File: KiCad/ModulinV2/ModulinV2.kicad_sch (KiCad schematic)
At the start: 0 parts

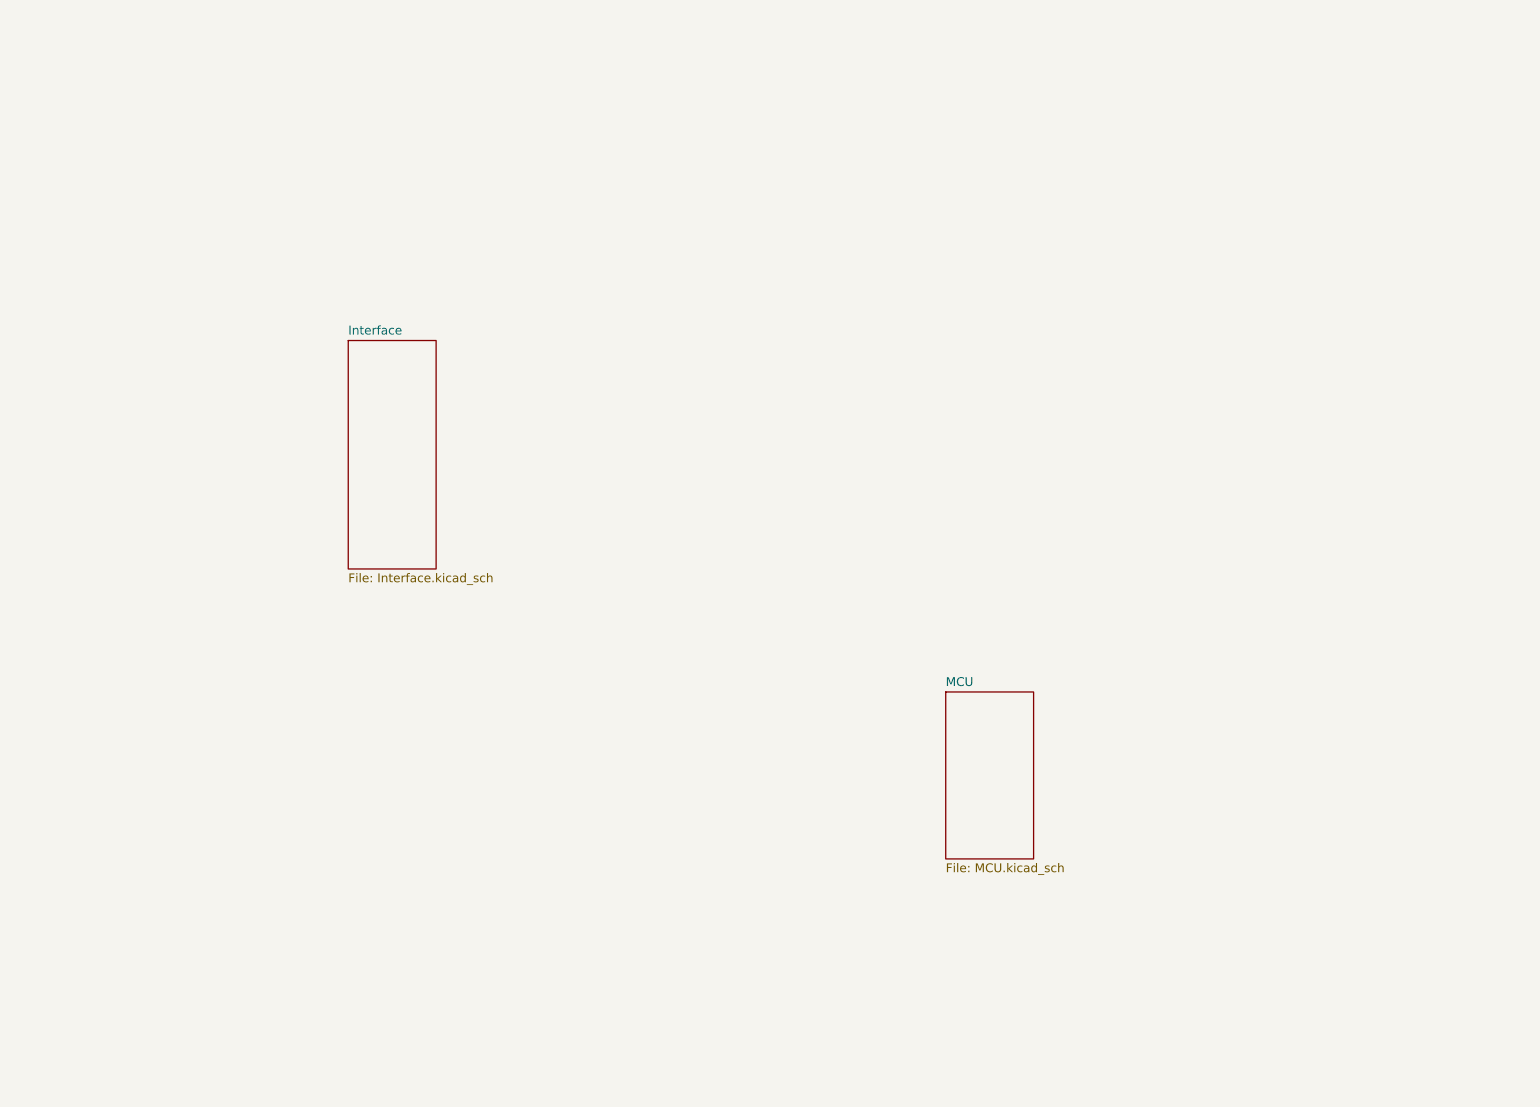
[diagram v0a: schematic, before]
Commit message: Added initial schematic and components for interface
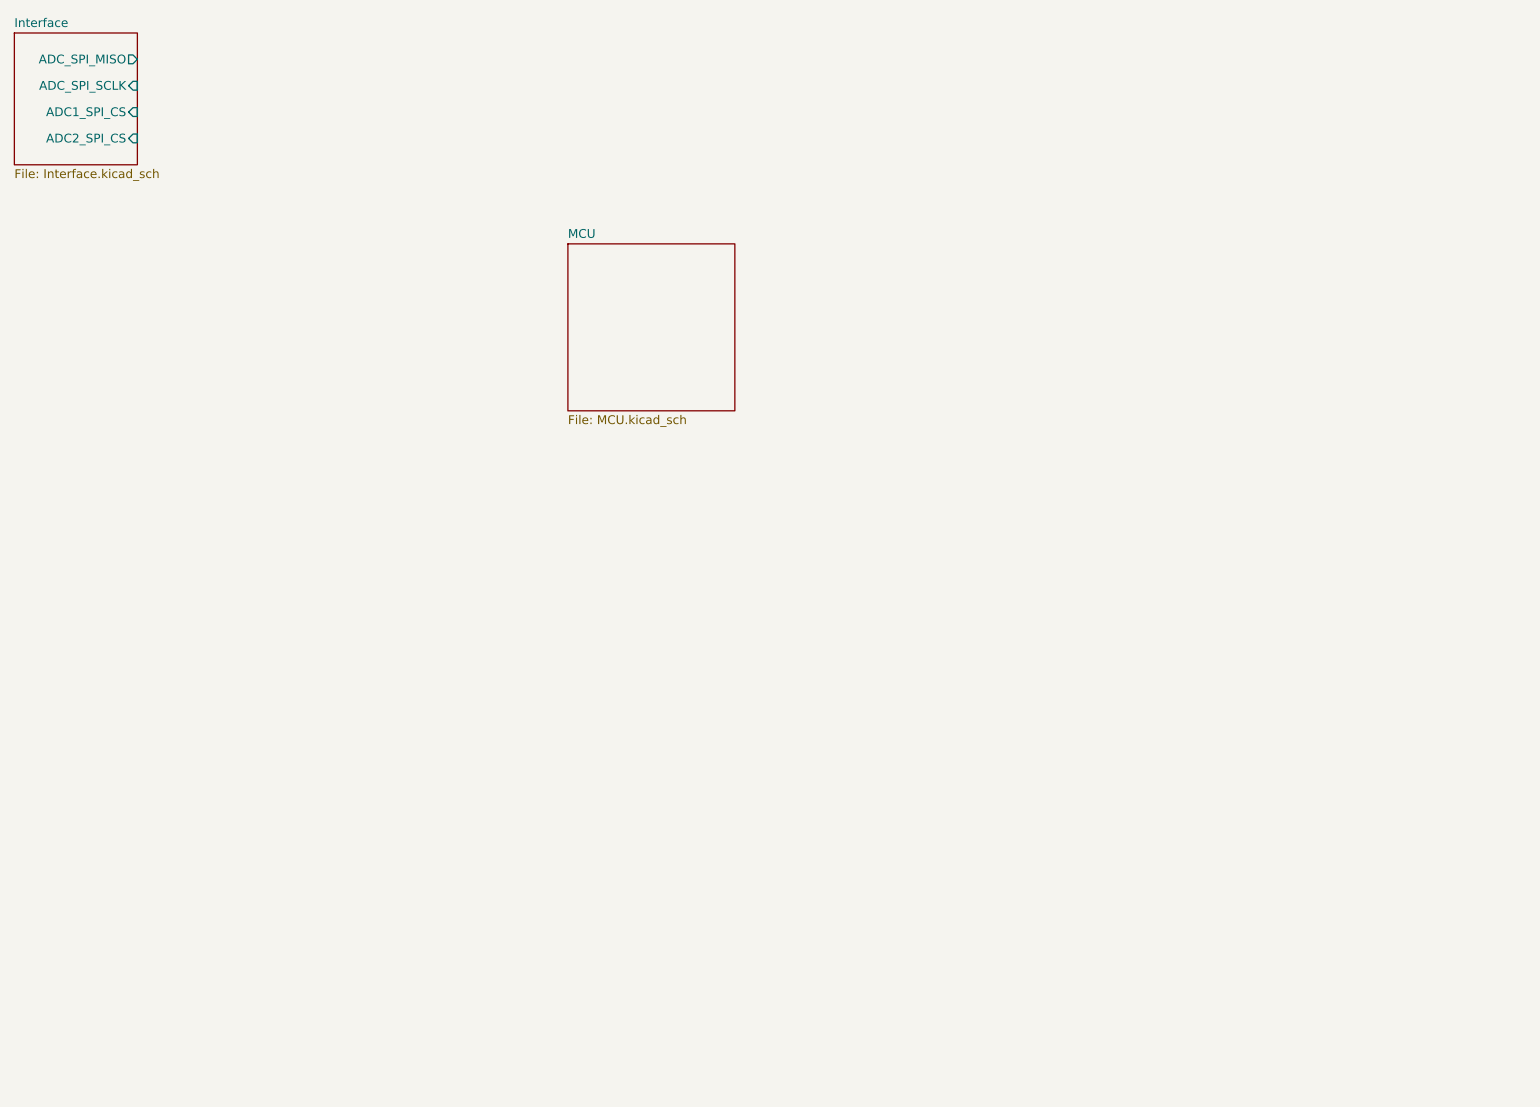
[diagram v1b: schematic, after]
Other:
- sheet Interface ports: added ADC1_SPI_CS, ADC2_SPI_CS, ADC_SPI_MISO, ADC_SPI_SCLK; removed none
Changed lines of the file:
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@@
 	)
 	(sheet
-		(at 69.85 72.39)
-		(size 12.7 33.02)
+		(at 21.59 27.94)
+		(size 17.78 19.05)
 		(exclude_from_sim no)
 		(in_bom yes)
@@
 		)
 		(property "Sheetname" "Interface"
-			(at 69.85 71.6784 0)
+			(at 21.59 27.2284 0)
 			(effects
 				(font
@@
 		)
 		(property "Sheetfile" "Interface.kicad_sch"
-			(at 69.85 105.9946 0)
+			(at 21.59 47.5746 0)
 			(effects
 				(font
@@
 				)
 				(justify left top)
+			)
+		)
+		(pin "ADC1_SPI_CS" input
+			(at 39.37 39.37 0)
+			(effects
+				(font
+					(size 1.27 1.27)
+				)
+				(justify right)
+			)
+		)
+		(pin "ADC_SPI_SCLK" input
+			(at 39.37 35.56 0)
+			(effects
+				(font
+					(size 1.27 1.27)
+				)
+				(justify right)
+			)
+		)
+		(pin "ADC_SPI_MISO" output
+			(at 39.37 31.75 0)
+			(effects
+				(font
+					(size 1.27 1.27)
+				)
+				(justify right)
+			)
+		)
+		(pin "ADC2_SPI_CS" input
+			(at 39.37 43.18 0)
+			(effects
+				(font
+					(size 1.27 1.27)
+				)
+				(justify right)
 			)
 		)
@@
 	)
 	(sheet
-		(at 156.21 123.19)
-		(size 12.7 24.13)
+		(at 101.6 58.42)
+		(size 24.13 24.13)
 		(exclude_from_sim no)
 		(in_bom yes)
@@
 		)
 		(property "Sheetname" "MCU"
-			(at 156.21 122.4784 0)
+			(at 101.6 57.7084 0)
 			(show_name yes)
 			(effects
@@
 		)
 		(property "Sheetfile" "MCU.kicad_sch"
-			(at 156.21 147.9046 0)
+			(at 101.6 83.1346 0)
 			(effects
 				(font

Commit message: Semi-finished interface schematic
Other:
- sheet Interface ports: added DAC1_SPI_CS, DAC1_SPI_MOSI, DAC2_SPI_CS, DAC_SPI_CLK, INTERFACE_PITCH_CV1, INTERFACE_PITCH_CV2, NOTE_TRIG1, NOTE_TRIG2, PRESSURE_CV1, PRESSURE_CV2; removed none
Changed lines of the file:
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@@
 	)
 	(sheet
-		(at 21.59 27.94)
-		(size 17.78 19.05)
+		(at 21.59 29.21)
+		(size 43.18 38.1)
 		(exclude_from_sim no)
 		(in_bom yes)
@@
 		)
 		(property "Sheetname" "Interface"
-			(at 21.59 27.2284 0)
+			(at 21.59 28.4984 0)
 			(effects
 				(font
@@
 		)
 		(property "Sheetfile" "Interface.kicad_sch"
-			(at 21.59 47.5746 0)
+			(at 21.59 67.8946 0)
 			(effects
 				(font
@@
 		)
 		(pin "ADC1_SPI_CS" input
-			(at 39.37 39.37 0)
+			(at 64.77 39.37 0)
 			(effects
 				(font
@@
 		)
 		(pin "ADC_SPI_SCLK" input
-			(at 39.37 35.56 0)
+			(at 64.77 35.56 0)
 			(effects
 				(font
@@
 		)
 		(pin "ADC_SPI_MISO" output
-			(at 39.37 31.75 0)
+			(at 64.77 31.75 0)
 			(effects
 				(font
@@
 		)
 		(pin "ADC2_SPI_CS" input
-			(at 39.37 43.18 0)
+			(at 64.77 43.18 0)
 			(effects
 				(font
@@
 				)
 				(justify right)
+			)
+		)
+		(pin "PRESSURE_CV1" output
+			(at 64.77 50.8 0)
+			(effects
+				(font
+					(size 1.27 1.27)
+				)
+				(justify right)
+			)
+		)
+		(pin "DAC1_SPI_MOSI" input
+			(at 21.59 31.75 180)
+			(effects
+				(font
+					(size 1.27 1.27)
+				)
+				(justify left)
+			)
+		)
+		(pin "INTERFACE_PITCH_CV2" output
+			(at 21.59 54.61 180)
+			(effects
+				(font
+					(size 1.27 1.27)
+				)
+				(justify left)
+			)
+		)
+		(pin "PRESSURE_CV2" output
+			(at 64.77 54.61 0)
+			(effects
+				(font
+					(size 1.27 1.27)
+				)
+				(justify right)
+			)
+		)
+		(pin "DAC1_SPI_CS" input
+			(at 21.59 39.37 180)
+			(effects
+				(font
+					(size 1.27 1.27)
+				)
+				(justify left)
+			)
+		)
+		(pin "NOTE_TRIG2" output
+			(at 64.77 64.77 0)
+			(effects
+				(font
+					(size 1.27 1.27)
+				)
+				(justify right)
+			)
+		)
+		(pin "DAC2_SPI_CS" input
+			(at 21.59 43.18 180)
+			(effects
+				(font
+					(size 1.27 1.27)
+				)
+				(justify left)
+			)
+		)
+		(pin "NOTE_TRIG1" output
+			(at 64.77 60.96 0)
+			(effects
+				(font
+					(size 1.27 1.27)
+				)
+				(justify right)
+			)
+		)
+		(pin "DAC_SPI_CLK" input
+			(at 21.59 35.56 180)
+			(effects
+				(font
+					(size 1.27 1.27)
+				)
+				(justify left)
+			)
+		)
+		(pin "INTERFACE_PITCH_CV1" output
+			(at 21.59 50.8 180)
+			(effects
+				(font
+					(size 1.27 1.27)
+				)
+				(justify left)
 			)
 		)
@@
 	)
 	(sheet
-		(at 101.6 58.42)
+		(at 102.87 36.83)
 		(size 24.13 24.13)
 		(exclude_from_sim no)
@@
 		)
 		(property "Sheetname" "MCU"
-			(at 101.6 57.7084 0)
+			(at 102.87 36.1184 0)
 			(show_name yes)
 			(effects
@@
 		)
 		(property "Sheetfile" "MCU.kicad_sch"
-			(at 101.6 83.1346 0)
+			(at 102.87 61.5446 0)
 			(effects
 				(font

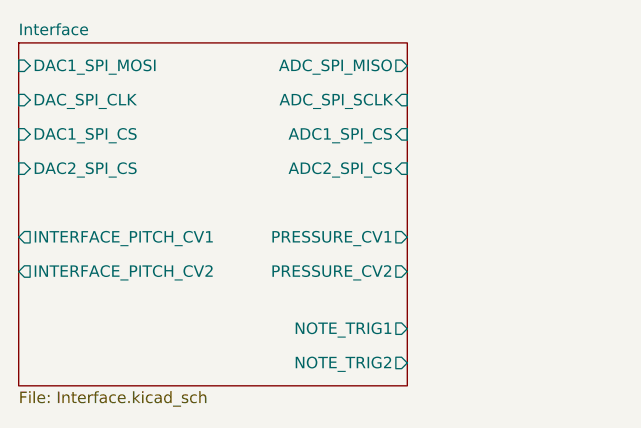
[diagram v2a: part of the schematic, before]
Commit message: Added CubeIDE folder and mapped out initial SPI pins
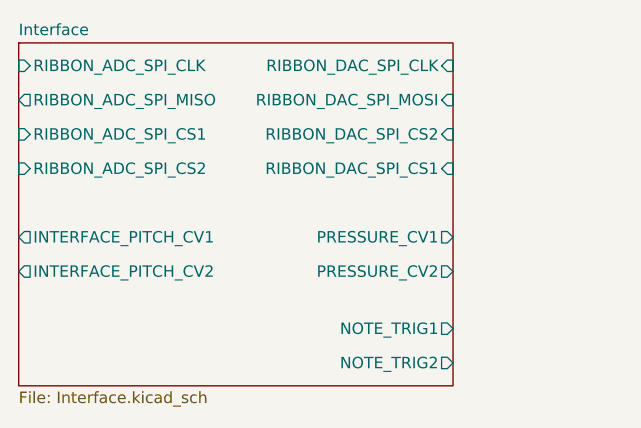
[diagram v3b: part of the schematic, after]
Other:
- sheet Interface ports: added RIBBON_ADC_SPI_CLK, RIBBON_ADC_SPI_CS1, RIBBON_ADC_SPI_CS2, RIBBON_ADC_SPI_MISO, RIBBON_DAC_SPI_CLK, RIBBON_DAC_SPI_CS1, RIBBON_DAC_SPI_CS2, RIBBON_DAC_SPI_MOSI; removed ADC1_SPI_CS, ADC2_SPI_CS, ADC_SPI_MISO, ADC_SPI_SCLK, DAC1_SPI_CS, DAC1_SPI_MOSI, DAC2_SPI_CS, DAC_SPI_CLK
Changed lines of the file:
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@@
 	(sheet
 		(at 21.59 29.21)
-		(size 43.18 38.1)
+		(size 48.26 38.1)
 		(exclude_from_sim no)
 		(in_bom yes)
@@
 			)
 		)
-		(pin "ADC1_SPI_CS" input
-			(at 64.77 39.37 0)
+		(pin "PRESSURE_CV1" output
+			(at 69.85 50.8 0)
 			(effects
 				(font
@@
 				)
 				(justify right)
-			)
-		)
-		(pin "ADC_SPI_SCLK" input
-			(at 64.77 35.56 0)
-			(effects
-				(font
-					(size 1.27 1.27)
-				)
-				(justify right)
-			)
-		)
-		(pin "ADC_SPI_MISO" output
-			(at 64.77 31.75 0)
-			(effects
-				(font
-					(size 1.27 1.27)
-				)
-				(justify right)
-			)
-		)
-		(pin "ADC2_SPI_CS" input
-			(at 64.77 43.18 0)
-			(effects
-				(font
-					(size 1.27 1.27)
-				)
-				(justify right)
-			)
-		)
-		(pin "PRESSURE_CV1" output
-			(at 64.77 50.8 0)
-			(effects
-				(font
-					(size 1.27 1.27)
-				)
-				(justify right)
-			)
-		)
-		(pin "DAC1_SPI_MOSI" input
-			(at 21.59 31.75 180)
-			(effects
-				(font
-					(size 1.27 1.27)
-				)
-				(justify left)
 			)
 		)
@@
 		)
 		(pin "PRESSURE_CV2" output
-			(at 64.77 54.61 0)
+			(at 69.85 54.61 0)
 			(effects
 				(font
@@
 			)
 		)
-		(pin "DAC1_SPI_CS" input
+		(pin "NOTE_TRIG2" output
+			(at 69.85 64.77 0)
+			(effects
+				(font
+					(size 1.27 1.27)
+				)
+				(justify right)
+			)
+		)
+		(pin "NOTE_TRIG1" output
+			(at 69.85 60.96 0)
+			(effects
+				(font
+					(size 1.27 1.27)
+				)
+				(justify right)
+			)
+		)
+		(pin "INTERFACE_PITCH_CV1" output
+			(at 21.59 50.8 180)
+			(effects
+				(font
+					(size 1.27 1.27)
+				)
+				(justify left)
+			)
+		)
+		(pin "RIBBON_ADC_SPI_CLK" input
+			(at 21.59 31.75 180)
+			(effects
+				(font
+					(size 1.27 1.27)
+				)
+				(justify left)
+			)
+		)
+		(pin "RIBBON_DAC_SPI_CLK" input
+			(at 69.85 31.75 0)
+			(effects
+				(font
+					(size 1.27 1.27)
+				)
+				(justify right)
+			)
+		)
+		(pin "RIBBON_ADC_SPI_CS1" input
 			(at 21.59 39.37 180)
 			(effects
@@
 			)
 		)
-		(pin "NOTE_TRIG2" output
-			(at 64.77 64.77 0)
+		(pin "RIBBON_DAC_SPI_CS1" input
+			(at 69.85 43.18 0)
 			(effects
 				(font
@@
 			)
 		)
-		(pin "DAC2_SPI_CS" input
-			(at 21.59 43.18 180)
-			(effects
-				(font
-					(size 1.27 1.27)
-				)
-				(justify left)
-			)
-		)
-		(pin "NOTE_TRIG1" output
-			(at 64.77 60.96 0)
+		(pin "RIBBON_DAC_SPI_MOSI" input
+			(at 69.85 35.56 0)
 			(effects
 				(font
@@
 			)
 		)
-		(pin "DAC_SPI_CLK" input
+		(pin "RIBBON_DAC_SPI_CS2" input
+			(at 69.85 39.37 0)
+			(effects
+				(font
+					(size 1.27 1.27)
+				)
+				(justify right)
+			)
+		)
+		(pin "RIBBON_ADC_SPI_MISO" output
 			(at 21.59 35.56 180)
 			(effects
@@
 			)
 		)
-		(pin "INTERFACE_PITCH_CV1" output
-			(at 21.59 50.8 180)
+		(pin "RIBBON_ADC_SPI_CS2" input
+			(at 21.59 43.18 180)
 			(effects
 				(font

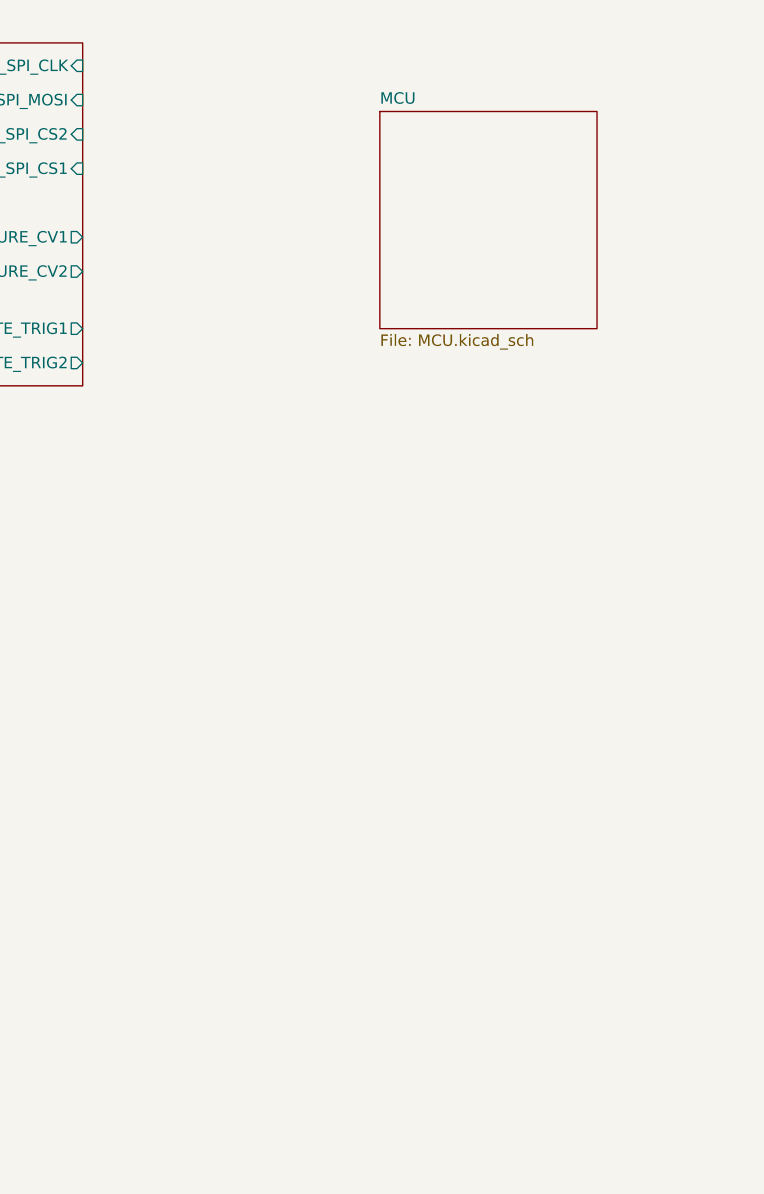
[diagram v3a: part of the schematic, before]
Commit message: Added initial schematic of VCO and repaired some schematic issues
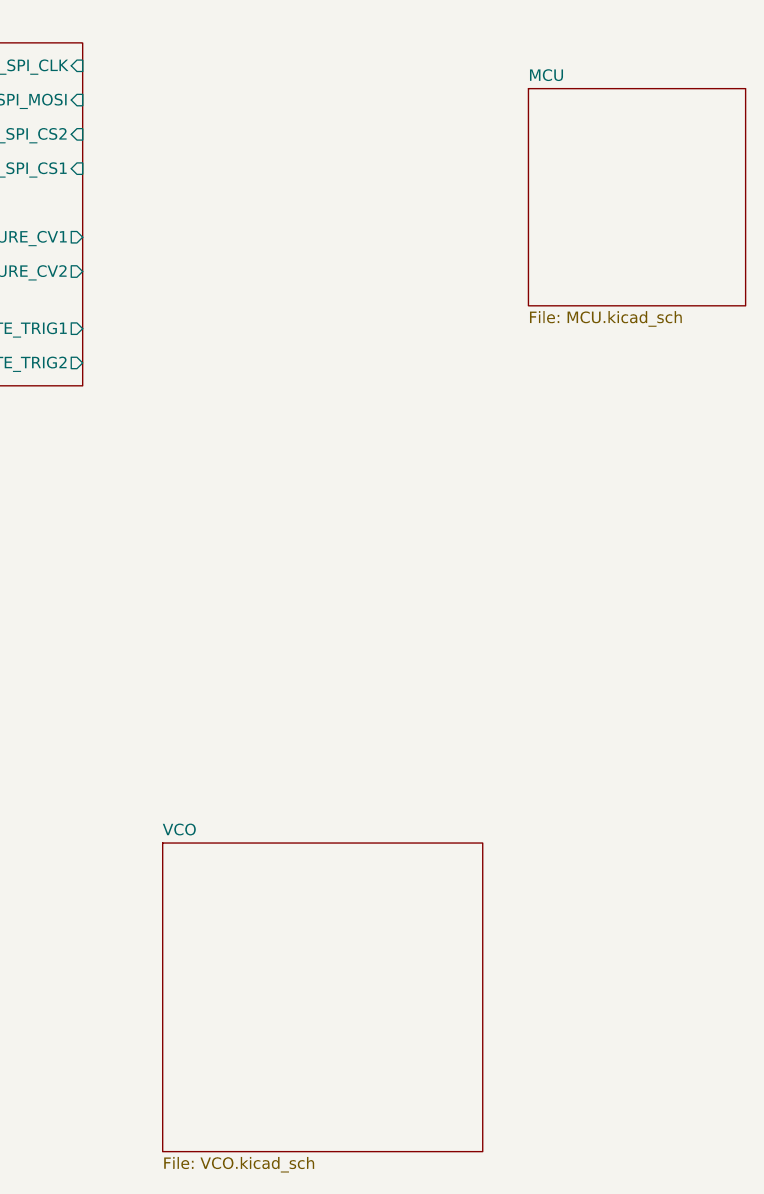
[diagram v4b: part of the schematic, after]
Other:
- added sheet VCO (VCO.kicad_sch)
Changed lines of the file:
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@@
 	)
 	(sheet
-		(at 102.87 36.83)
+		(at 119.38 34.29)
 		(size 24.13 24.13)
 		(exclude_from_sim no)
@@
 		)
 		(property "Sheetname" "MCU"
-			(at 102.87 36.1184 0)
+			(at 119.38 33.5784 0)
 			(show_name yes)
 			(effects
@@
 		)
 		(property "Sheetfile" "MCU.kicad_sch"
-			(at 102.87 61.5446 0)
+			(at 119.38 59.0046 0)
 			(effects
 				(font
@@
 				)
 			)
+		)
+	)
+	(sheet
+		(at 78.74 118.11)
+		(size 35.56 34.29)
+		(exclude_from_sim no)
+		(in_bom yes)
+		(on_board yes)
+		(dnp no)
+		(fields_autoplaced yes)
+		(stroke
+			(width 0.1524)
+			(type solid)
+		)
+		(fill
+			(color 0 0 0 0.0000)
+		)
+		(property "Sheetname" "VCO"
+			(at 78.74 117.3984 0)
+			(effects
+				(font
+					(size 1.27 1.27)
+				)
+				(justify left bottom)
+			)
+		)
+		(property "Sheetfile" "VCO.kicad_sch"
+			(at 78.74 152.9846 0)
+			(effects
+				(font
+					(size 1.27 1.27)
+				)
+				(justify left top)
+			)
+		)
+		(instances
+			(project "ModulinV2"
+				(path "/c6b34a57-3941-4b56-8b80-1848c7f41082"
+					(page "4")
+				)
+			)
